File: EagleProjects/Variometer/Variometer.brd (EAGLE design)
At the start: 100 x 51 mm, 41 parts, among them Q1 2N7000

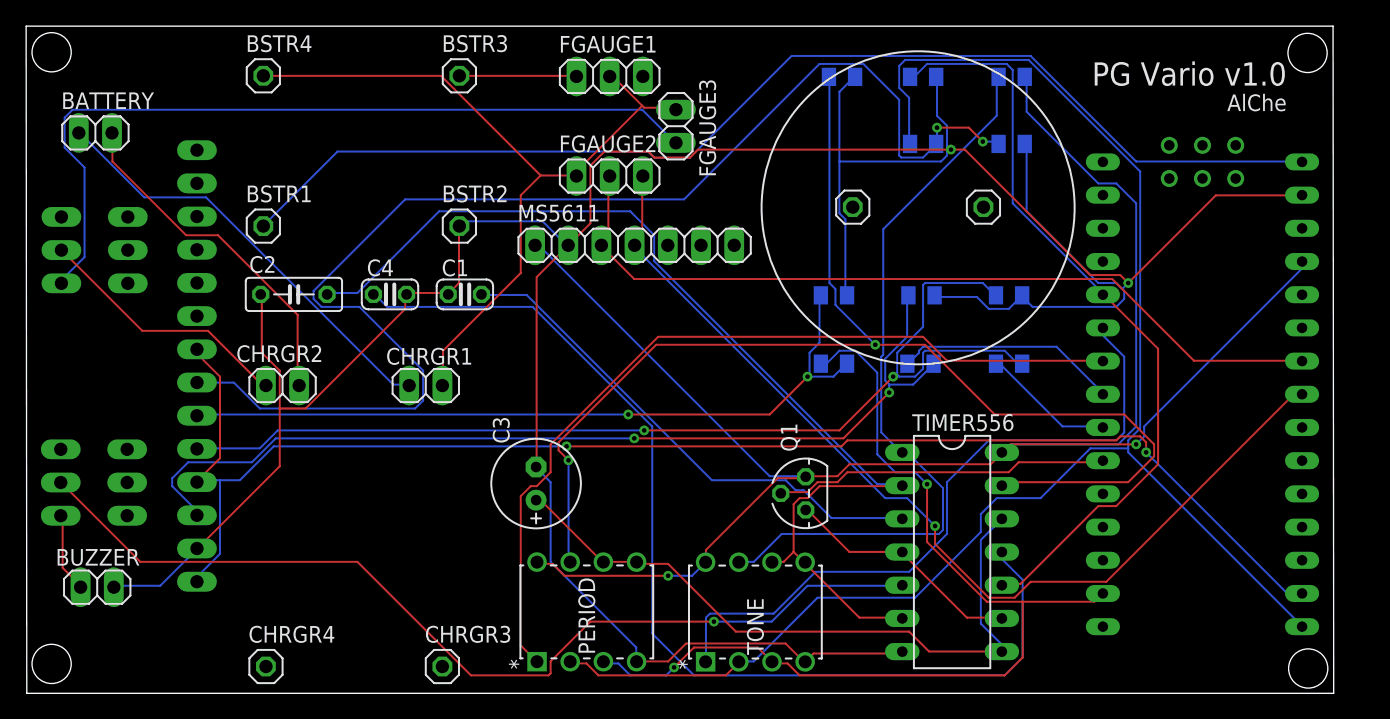
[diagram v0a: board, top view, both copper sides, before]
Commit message: Eagle Project v1.1
Fixed pcb bugs in v1.0 version
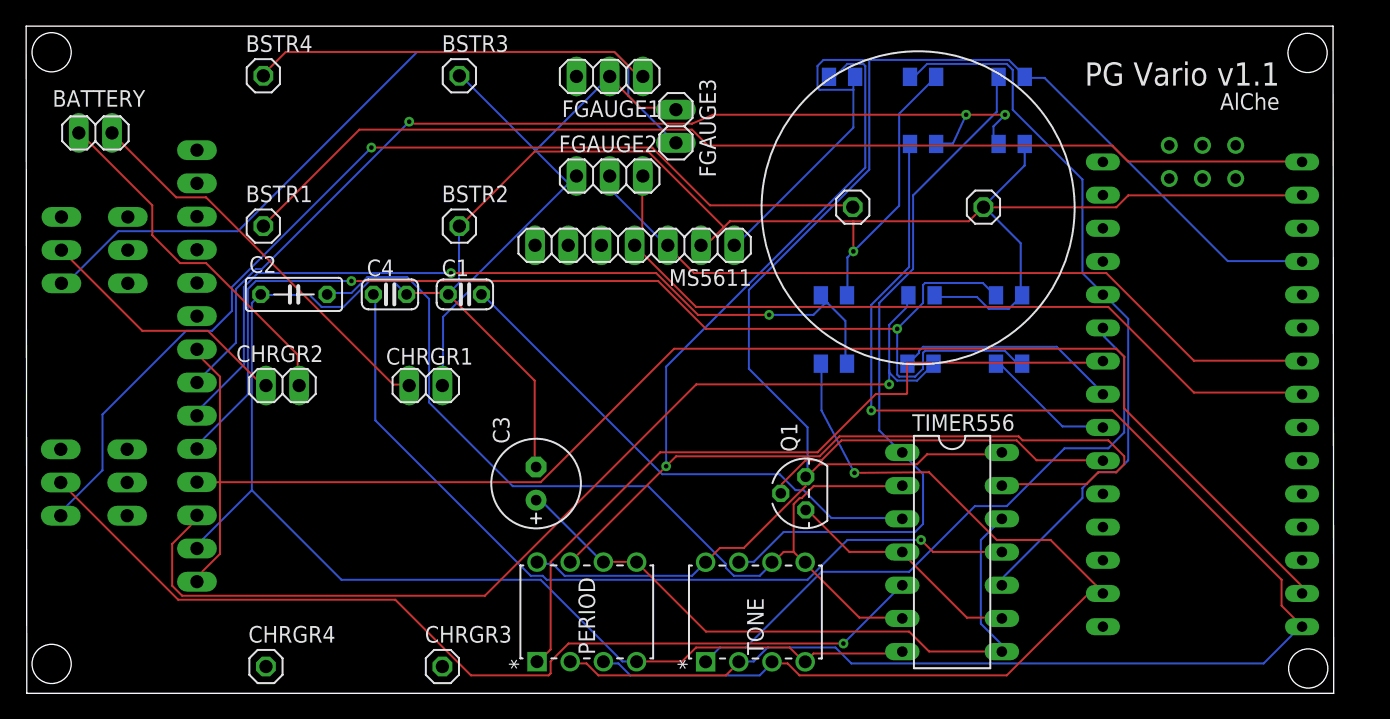
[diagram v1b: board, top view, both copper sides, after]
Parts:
- removed BUZZER: (no value), pinhead:1X02
- turned BATTERY to 180 degrees
- turned FGAUGE1 to 180 degrees
- turned MS5611 to 180 degrees
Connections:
- removed net BZR_TRMNL: BUZZER.2, BZR_BTN.1
- new net BZR_SIGNAL: BZR_BTN.1, BZR_PIN1.1
- net BSTR_VIN: now also BSTR4.1; no longer BSTR3.1
- net CHARGER_GND: now also BSTR3.1; no longer BSTR4.1
- net GND: now also BZR_PIN2.1; no longer BUZZER.1, R3.1
- net VCC: now also R3.1
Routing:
- net BZR_SIGNAL: track 0.00 -> 77.9 mm, vias 0 -> 1
- net GND: track 254.6 -> 231.8 mm, vias 2 -> 1
- net BSTR_VIN: track 8.97 -> 30.6 mm
- net TFT_SPI-SCK: track 99.2 -> 79.3 mm, vias 2 -> 3
- net N$6: track 80.3 -> 64.4 mm, vias 0 -> 1
- net SDA: track 75.2 -> 61.5 mm, vias 1 -> 0
- net CHARGER_GND: track 60.3 -> 47.1 mm
- net TFT_DC: track 81.3 -> 90.6 mm
- net N$1: track 81.5 -> 74.4 mm
- net TFT_SPI-MOSI: track 57.9 -> 65.0 mm
- net 3.3V: track 111.6 -> 118.4 mm, vias 2 -> 0
- net N$15: track 64.8 -> 58.2 mm
- net TFT_CS: track 73.6 -> 79.8 mm, vias 2 -> 1
- net BZR_TRMNL: track 6.16 -> 0.00 mm
- net BSTR_VOUT: track 88.6 -> 83.6 mm
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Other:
- board text added: "PG Vario v1.1"
- board text removed: "PG Vario v1.0"
